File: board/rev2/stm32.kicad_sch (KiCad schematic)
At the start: 2 parts, among them U5 STM32U575VGTx, U7 TPD6S300A

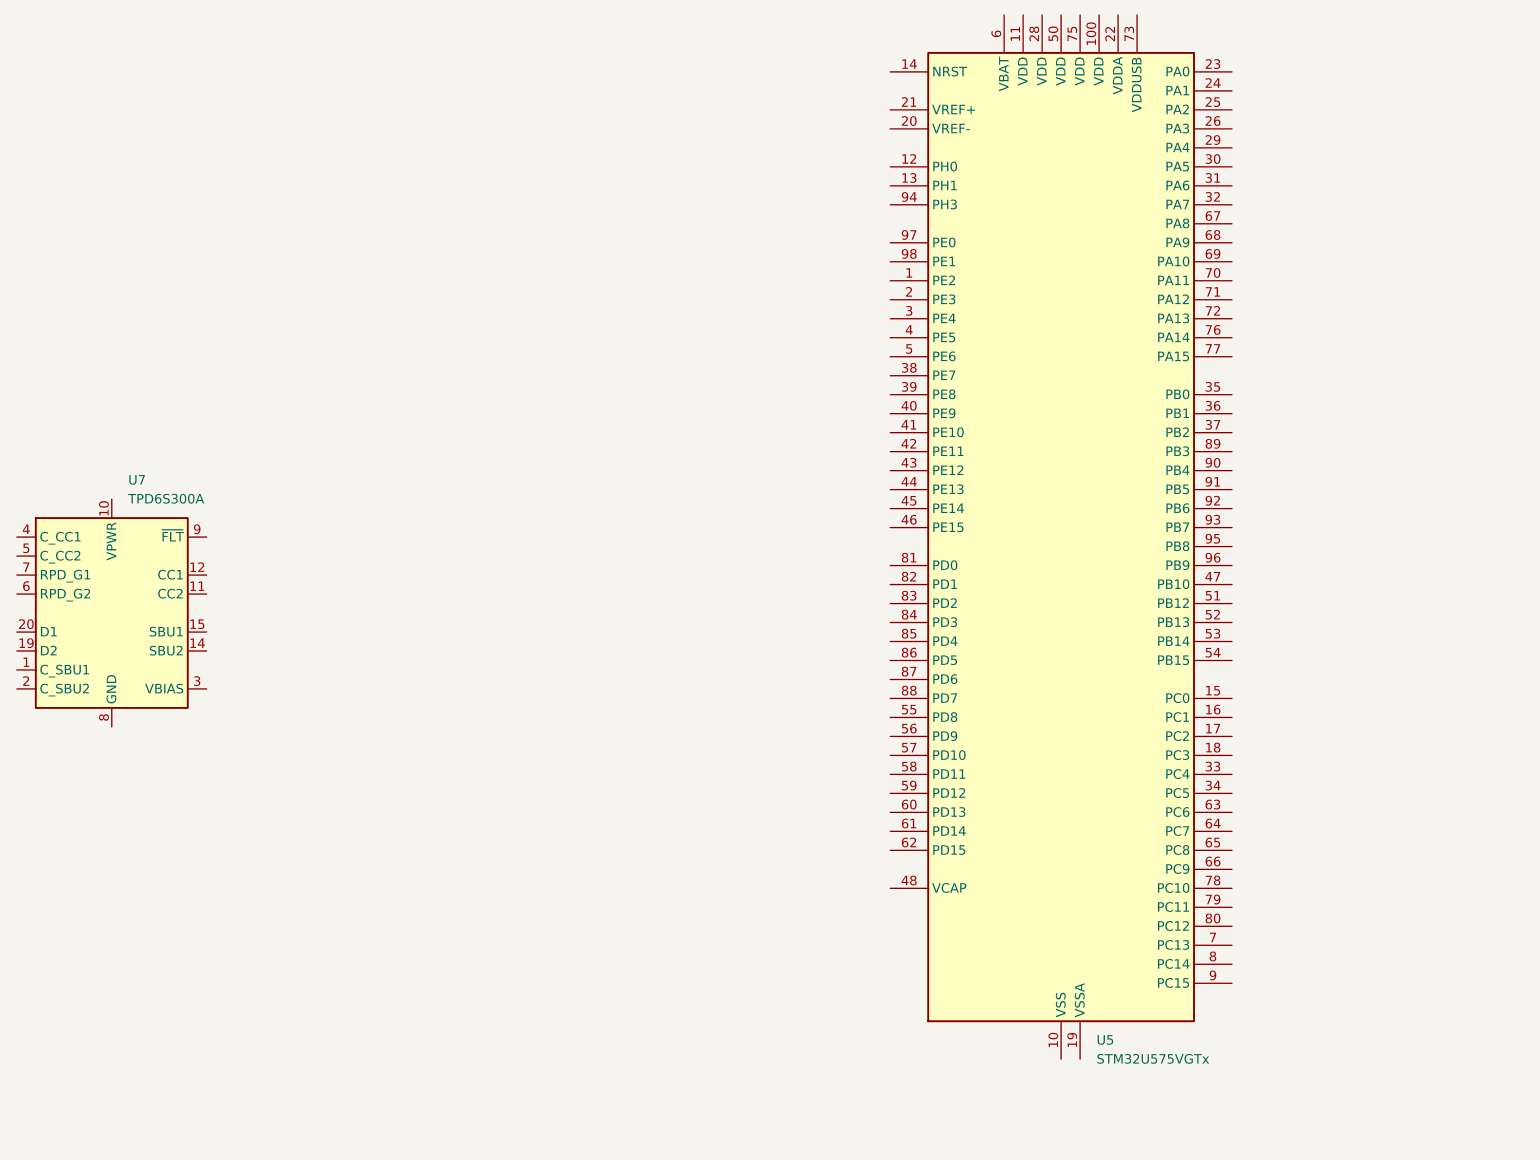
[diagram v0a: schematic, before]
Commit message: Finish most of power section of rev2 PCB
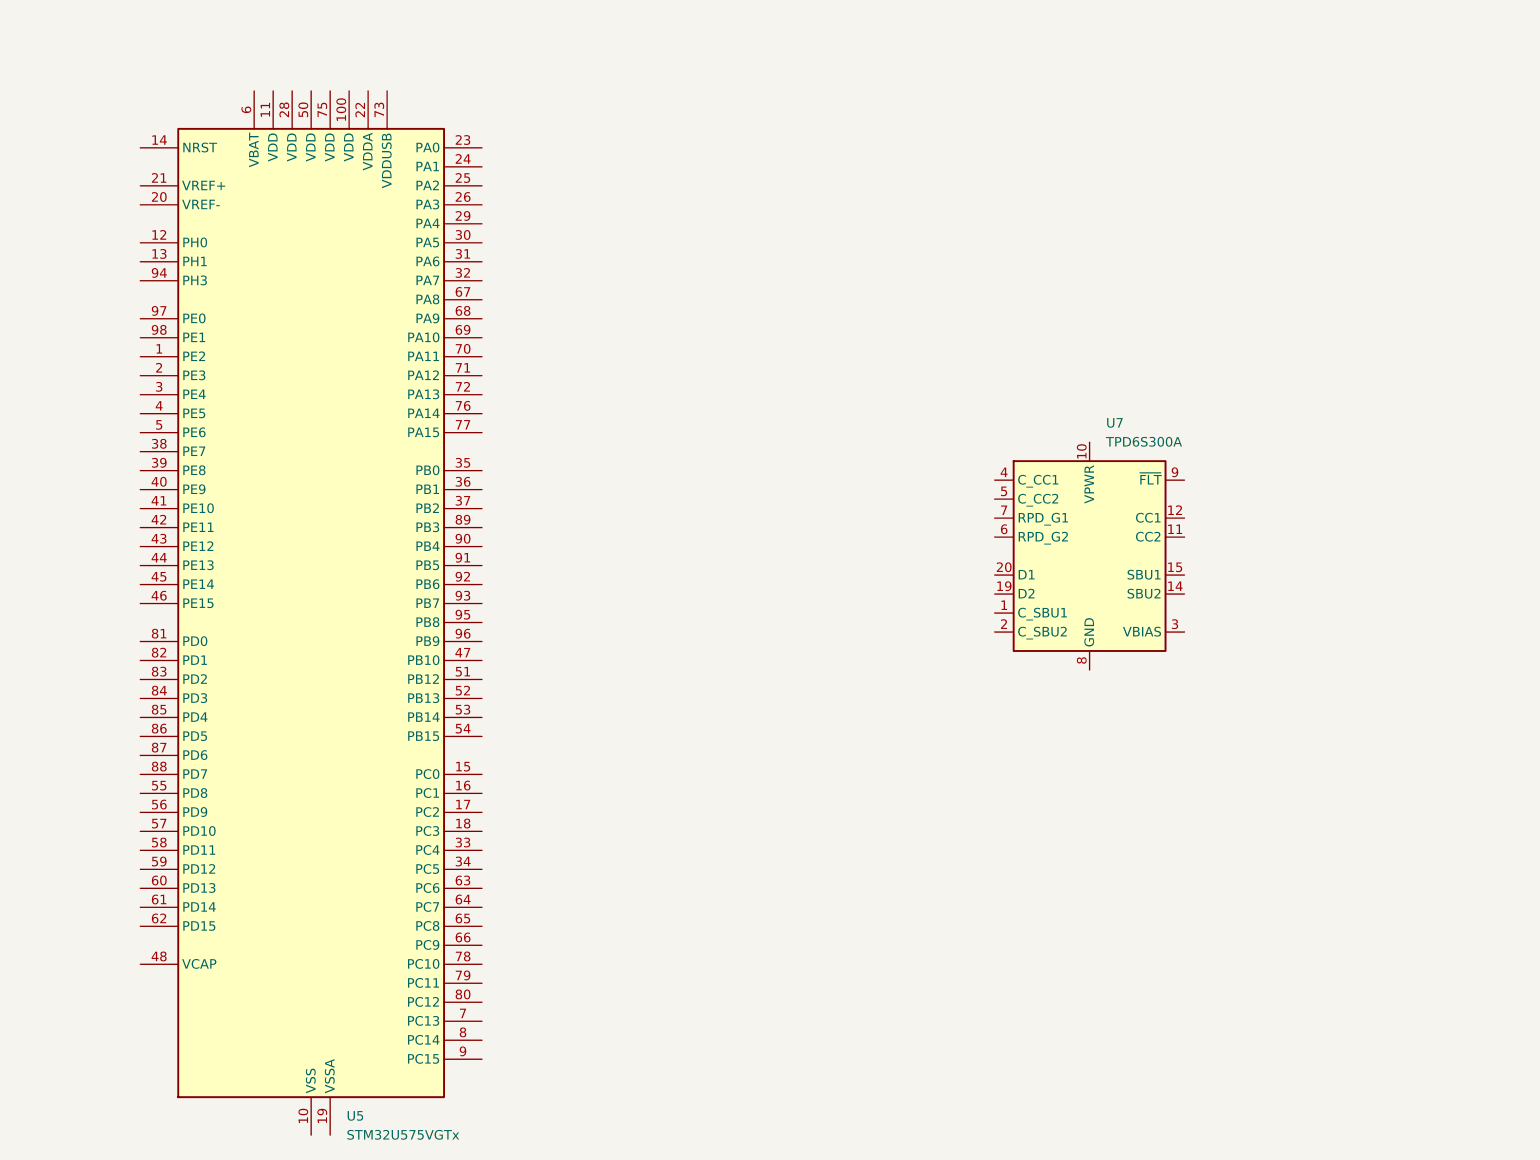
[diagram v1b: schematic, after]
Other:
- moved on the sheet: U5, U7
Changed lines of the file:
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@@
 	(symbol
 		(lib_id "MCU_ST_STM32U5:STM32U575VGTx")
-		(at 200.66 90.17 0)
+		(at 100.33 100.33 0)
 		(unit 1)
 		(exclude_from_sim no)
@@
 		(fields_autoplaced yes)
 		(property "Reference" "U5"
-			(at 205.3941 156.21 0)
+			(at 105.0641 166.37 0)
 			(effects
 				(font
@@
 		)
 		(property "Value" "STM32U575VGTx"
-			(at 205.3941 158.75 0)
+			(at 105.0641 168.91 0)
 			(effects
 				(font
@@
 		)
 		(property "Footprint" "Package_QFP:LQFP-100_14x14mm_P0.5mm"
-			(at 182.88 153.67 0)
+			(at 82.55 163.83 0)
 			(effects
 				(font
@@
 		)
 		(property "Datasheet" "https://www.st.com/resource/en/datasheet/stm32u575vg.pdf"
-			(at 200.66 90.17 0)
+			(at 100.33 100.33 0)
 			(effects
 				(font
@@
 		)
 		(property "Description" "STMicroelectronics Arm Cortex-M33 MCU, 1024KB flash, 786KB RAM, 160 MHz, 1.71-3.6V, 82 GPIO, LQFP100"
-			(at 200.66 90.17 0)
+			(at 100.33 100.33 0)
 			(effects
 				(font
@@
 	(symbol
 		(lib_id "Power_Protection:TPD6S300A")
-		(at 73.66 99.06 0)
+		(at 204.47 91.44 0)
 		(unit 1)
 		(exclude_from_sim no)
@@
 		(fields_autoplaced yes)
 		(property "Reference" "U7"
-			(at 75.8541 81.28 0)
+			(at 206.6641 73.66 0)
 			(effects
 				(font
@@
 		)
 		(property "Value" "TPD6S300A"
-			(at 75.8541 83.82 0)
+			(at 206.6641 76.2 0)
 			(effects
 				(font
@@
 		)
 		(property "Footprint" "Package_DFN_QFN:WQFN-20-1EP_3x3mm_P0.4mm_EP1.7x1.7mm_ThermalVias"
-			(at 73.66 124.46 0)
+			(at 204.47 116.84 0)
 			(effects
 				(font
@@
 		)
 		(property "Datasheet" "https://www.ti.com/lit/ds/symlink/tpd6s300a.pdf"
-			(at 73.66 127 0)
+			(at 204.47 119.38 0)
 			(effects
 				(font
@@
 		)
 		(property "Description" "USB Type-C Port Protector: Short-to-VBUS Overvoltage and IEC ESD Protection, WQFN-20"
-			(at 73.66 99.06 0)
-			(effects
-				(font
+			(at 204.47 91.44 0)
+			(effects
+				(font

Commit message: More board work
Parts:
- added C26: 100nF, symbol Device:C_Small
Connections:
- net USB_D+: now reaches U7.1 (C_SBU1)
- net VDD: now reaches U7.10 (VPWR)
- net GND: now reaches U7.19 (D2)
- net GND: now also U7.20 (D1), C26.2
- net USB_D-: now reaches U7.2 (C_SBU2)
- net at U7.3 (VBIAS): now also C26.1
- net USB_CC1: now reaches U7.4 (C_CC1)
- net USB_CC1: now also U7.7 (RPD_G1)
- net USB_CC2: now reaches U7.5 (C_CC2)
- net USB_CC2: now also U7.6 (RPD_G2)
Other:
- moved on the sheet: U7
